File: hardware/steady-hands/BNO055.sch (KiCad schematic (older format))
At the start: 8 parts

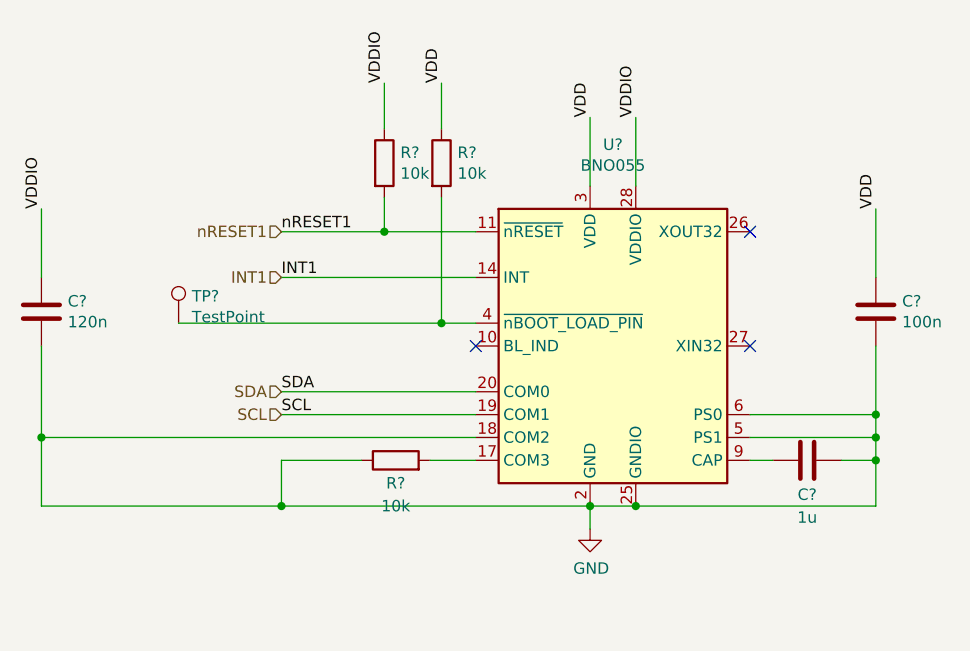
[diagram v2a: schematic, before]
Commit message: Completes schematic connections
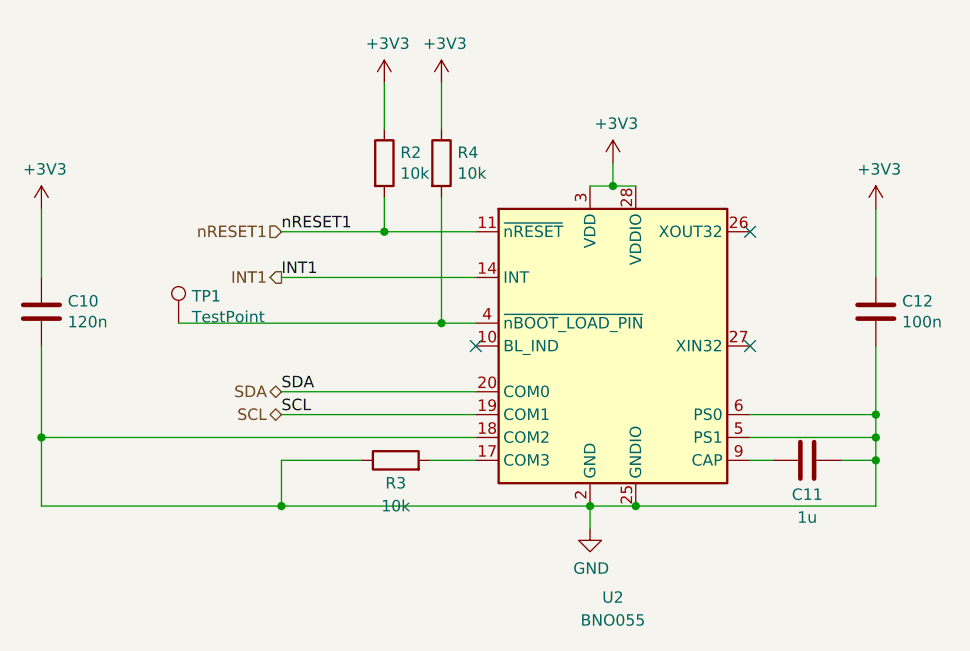
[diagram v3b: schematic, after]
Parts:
- gave numbers to parts that had none: 8
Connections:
- net VDDIO is gone; now on net +3V3: C10.1, R2.1, U2.28 (VDDIO)
- net VDD renamed +3V3
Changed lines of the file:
@@
 $Descr A4 11693 8268
 encoding utf-8
-Sheet 2 7
+Sheet 5 7
 Title ""
 Date ""
@@
 P 6300 3800
 AR Path="/5EF56CFF" Ref="U?"  Part="1"
-AR Path="/5EF43BAC/5EF56CFF" Ref="U?"  Part="1"
-F 0 "U?" H 6300 4681 50  0000 C CNN
-F 1 "BNO055" H 6300 4590 50  0000 C CNN
+AR Path="/5EF43BAC/5EF56CFF" Ref="U2"  Part="1"
+F 0 "U2" H 6300 2700 50  0000 C CNN
+F 1 "BNO055" H 6300 2600 50  0000 C CNN
 F 2 "Package_LGA:LGA-28_5.2x3.8mm_P0.5mm" H 6550 3150 50  0001 L CNN
 F 3 "https://ae-bst.resource.bosch.com/media/_tech/media/datasheets/BST_BNO055_DS000_14.pdf" H 6300 4000 50  0001 C CNN
@@
 $EndComp
 $Comp
-L power:GND #PWR?
+L power:GND #PWR0119
 U 1 1 5EF56D05
 P 6200 4600
-F 0 "#PWR?" H 6200 4350 50  0001 C CNN
+F 0 "#PWR0119" H 6200 4350 50  0001 C CNN
 F 1 "GND" H 6205 4427 50  0000 C CNN
 F 2 "" H 6200 4600 50  0001 C CNN
@@
 Connection ~ 6200 4500
 $Comp
-L Device:C C?
+L Device:C C11
 U 1 1 5EF56D0E
 P 7150 4300
-F 0 "C?" V 7300 4300 50  0000 C CNN
+F 0 "C11" V 7300 4300 50  0000 C CNN
 F 1 "1u" V 7400 4300 50  0000 C CNN
 F 2 "" H 7188 4150 50  0001 C CNN
@@
 Connection ~ 7450 4200
 $Comp
-L Device:R R?
+L Device:R R2
 U 1 1 5EF56D1E
 P 5300 3000
-F 0 "R?" H 5370 3046 50  0000 L CNN
+F 0 "R2" H 5370 3046 50  0000 L CNN
 F 1 "10k" H 5370 2955 50  0000 L CNN
 F 2 "" V 5230 3000 50  0001 C CNN
@@
 $EndComp
 $Comp
-L Device:C C?
+L Device:C C10
 U 1 1 5EF56D2A
 P 3800 3650
-F 0 "C?" H 3915 3696 50  0000 L CNN
+F 0 "C10" H 3915 3696 50  0000 L CNN
 F 1 "120n" H 3915 3605 50  0000 L CNN
 F 2 "" H 3838 3500 50  0001 C CNN
@@
 $EndComp
 $Comp
-L Device:C C?
+L Device:C C12
 U 1 1 5EF56D56
 P 7450 3650
-F 0 "C?" H 7565 3696 50  0000 L CNN
+F 0 "C12" H 7565 3696 50  0000 L CNN
 F 1 "100n" H 7565 3605 50  0000 L CNN
 F 2 "" H 7488 3500 50  0001 C CNN
@@
 	7450 4100 7450 4200
 $Comp
-L Device:R R?
+L Device:R R4
 U 1 1 5EF56D5F
 P 5550 3000
-F 0 "R?" H 5620 3046 50  0000 L CNN
+F 0 "R4" H 5620 3046 50  0000 L CNN
 F 1 "10k" H 5620 2955 50  0000 L CNN
 F 2 "" V 5480 3000 50  0001 C CNN
@@
 Wire Wire Line
 	4850 3500 5700 3500
-Text Label 6400 2800 1    50   ~ 0
-VDDIO
-Text Label 6200 2800 1    50   ~ 0
-VDD
 Text Label 4850 3500 0    50   ~ 0
 INT1
 Text Label 4850 3300 0    50   ~ 0
 nRESET1
-Text Label 5550 2650 1    50   ~ 0
-VDD
-Text Label 7450 3200 1    50   ~ 0
-VDD
-Text Label 3800 3200 1    50   ~ 0
-VDDIO
-Wire Wire Line
-	6400 3100 6400 2800
-Wire Wire Line
-	6200 3100 6200 2800
 Text Label 4850 4100 0    50   ~ 0
 SCL
 Text Label 4850 4000 0    50   ~ 0
 SDA
-Text HLabel 4850 4000 0    50   Input ~ 0
+Text HLabel 4850 4000 0    50   BiDi ~ 0
 SDA
-Text HLabel 4850 4100 0    50   Input ~ 0
+Text HLabel 4850 4100 0    50   BiDi ~ 0
 SCL
-Text HLabel 4850 3500 0    50   Input ~ 0
+Text HLabel 4850 3500 0    50   Output ~ 0
 INT1
 Wire Wire Line
@@
 Wire Wire Line
 	4850 3300 5300 3300
-Text Label 5300 2650 1    50   ~ 0
-VDDIO
 Wire Wire Line
 	5300 2650 5300 2850
@@
 NoConn ~ 5700 3800
 $Comp
-L Connector:TestPoint TP?
+L Connector:TestPoint TP1
 U 1 1 5EFBEA12
 P 4400 3700
-F 0 "TP?" H 4458 3818 50  0000 L CNN
+F 0 "TP1" H 4458 3818 50  0000 L CNN
 F 1 "TestPoint" H 4458 3727 50  0000 L CNN
 F 2 "" H 4600 3700 50  0001 C CNN
@@
 	4400 3700 5550 3700
 $Comp
-L Device:R R?
+L Device:R R3
 U 1 1 5EFC1422
 P 5350 4300
-F 0 "R?" V 5250 4300 50  0000 C CNN
+F 0 "R3" V 5250 4300 50  0000 C CNN
 F 1 "10k" V 5150 4300 50  0000 C CNN
 F 2 "" V 5280 4300 50  0001 C CNN
@@
 Wire Wire Line
 	4850 4500 6200 4500
+Wire Wire Line
+	6200 3100 6300 3100
+Connection ~ 6300 3100
+Wire Wire Line
+	6300 3100 6400 3100
+Wire Wire Line
+	6300 3000 6300 3100
+$Comp
+L power:+3V3 #PWR0120
+U 1 1 5F16055B
+P 6300 3000
+F 0 "#PWR0120" H 6300 2850 50  0001 C CNN
+F 1 "+3V3" H 6315 3173 50  0000 C CNN
+F 2 "" H 6300 3000 50  0001 C CNN
+F 3 "" H 6300 3000 50  0001 C CNN
+	1    6300 3000
+	1    0    0    -1
+$EndComp
+$Comp
+L power:+3V3 #PWR0121
+U 1 1 5F1606C7
+P 7450 3200
+F 0 "#PWR0121" H 7450 3050 50  0001 C CNN
+F 1 "+3V3" H 7465 3373 50  0000 C CNN
+F 2 "" H 7450 3200 50  0001 C CNN
+F 3 "" H 7450 3200 50  0001 C CNN
+	1    7450 3200
+	1    0    0    -1
+$EndComp
+$Comp
+L power:+3V3 #PWR0122
+U 1 1 5F16088A
+P 5550 2650
+F 0 "#PWR0122" H 5550 2500 50  0001 C CNN
+F 1 "+3V3" H 5565 2823 50  0000 C CNN
+F 2 "" H 5550 2650 50  0001 C CNN
+F 3 "" H 5550 2650 50  0001 C CNN
+	1    5550 2650
+	1    0    0    -1
+$EndComp
+$Comp
+L power:+3V3 #PWR0123
+U 1 1 5F160A1A
+P 5300 2650
+F 0 "#PWR0123" H 5300 2500 50  0001 C CNN
+F 1 "+3V3" H 5315 2823 50  0000 C CNN
+F 2 "" H 5300 2650 50  0001 C CNN
+F 3 "" H 5300 2650 50  0001 C CNN
+	1    5300 2650
+	1    0    0    -1
+$EndComp
+$Comp
+L power:+3V3 #PWR0124
+U 1 1 5F160BBC
+P 3800 3200
+F 0 "#PWR0124" H 3800 3050 50  0001 C CNN
+F 1 "+3V3" H 3815 3373 50  0000 C CNN
+F 2 "" H 3800 3200 50  0001 C CNN
+F 3 "" H 3800 3200 50  0001 C CNN
+	1    3800 3200
+	1    0    0    -1
+$EndComp
 $EndSCHEMATC

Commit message: Edits label names and switch configuration
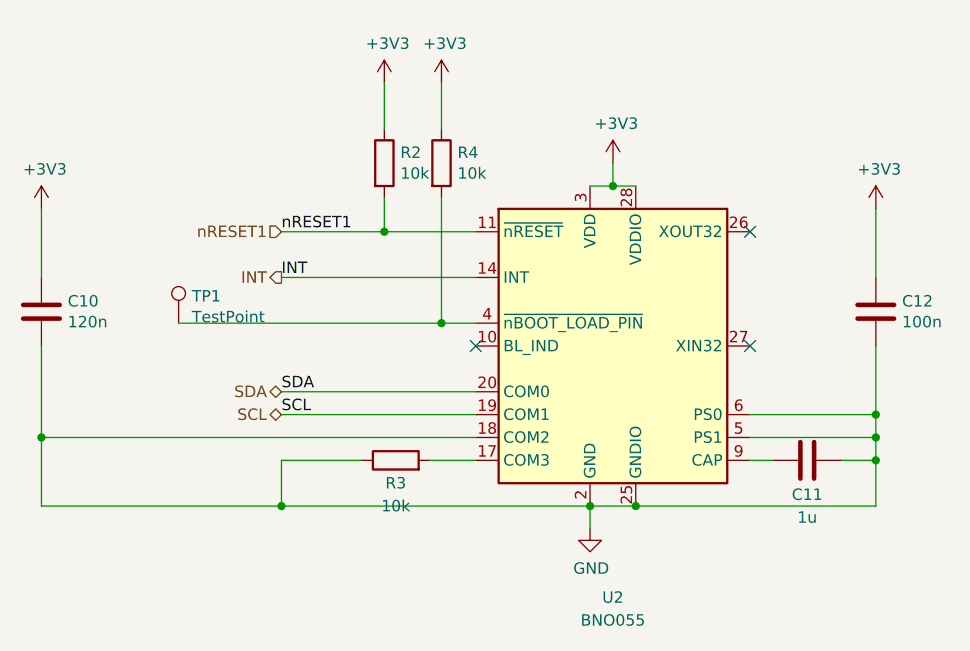
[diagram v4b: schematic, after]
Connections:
- net INT1 renamed INT
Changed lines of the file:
@@
 	4850 3500 5700 3500
 Text Label 4850 3500 0    50   ~ 0
-INT1
+INT
 Text Label 4850 3300 0    50   ~ 0
 nRESET1
@@
 SCL
 Text HLabel 4850 3500 0    50   Output ~ 0
-INT1
+INT
 Wire Wire Line
 	5300 3150 5300 3300

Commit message: Adds footprints
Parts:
- C10, C11, C12: footprint (none) -> Capacitor_SMD:C_0402_1005Metric
- R2, R3, R4: footprint (none) -> Resistor_SMD:R_0402_1005Metric
- TP1: footprint (none) -> TestPoint:TestPoint_Pad_D1.0mm
- U2: symbol Sensor_Motion:BNO055 -> steady-hands-rescue:BNO055-Sensor_Motion
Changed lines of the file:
@@
 $Descr A4 11693 8268
 encoding utf-8
-Sheet 5 7
+Sheet 4 6
 Title ""
 Date ""
@@
 $EndDescr
 $Comp
-L Sensor_Motion:BNO055 U?
+L steady-hands-rescue:BNO055-Sensor_Motion U?
 U 1 1 5EF56CFF
 P 6300 3800
@@
 F 0 "C11" V 7300 4300 50  0000 C CNN
 F 1 "1u" V 7400 4300 50  0000 C CNN
-F 2 "" H 7188 4150 50  0001 C CNN
+F 2 "Capacitor_SMD:C_0402_1005Metric" H 7188 4150 50  0001 C CNN
 F 3 "~" H 7150 4300 50  0001 C CNN
 	1    7150 4300
@@
 F 0 "R2" H 5370 3046 50  0000 L CNN
 F 1 "10k" H 5370 2955 50  0000 L CNN
-F 2 "" V 5230 3000 50  0001 C CNN
+F 2 "Resistor_SMD:R_0402_1005Metric" V 5230 3000 50  0001 C CNN
 F 3 "~" H 5300 3000 50  0001 C CNN
 	1    5300 3000
@@
 F 0 "C10" H 3915 3696 50  0000 L CNN
 F 1 "120n" H 3915 3605 50  0000 L CNN
-F 2 "" H 3838 3500 50  0001 C CNN
+F 2 "Capacitor_SMD:C_0402_1005Metric" H 3838 3500 50  0001 C CNN
 F 3 "~" H 3800 3650 50  0001 C CNN
 	1    3800 3650
@@
 F 0 "C12" H 7565 3696 50  0000 L CNN
 F 1 "100n" H 7565 3605 50  0000 L CNN
-F 2 "" H 7488 3500 50  0001 C CNN
+F 2 "Capacitor_SMD:C_0402_1005Metric" H 7488 3500 50  0001 C CNN
 F 3 "~" H 7450 3650 50  0001 C CNN
 	1    7450 3650
@@
 F 0 "R4" H 5620 3046 50  0000 L CNN
 F 1 "10k" H 5620 2955 50  0000 L CNN
-F 2 "" V 5480 3000 50  0001 C CNN
+F 2 "Resistor_SMD:R_0402_1005Metric" V 5480 3000 50  0001 C CNN
 F 3 "~" H 5550 3000 50  0001 C CNN
 	1    5550 3000
@@
 F 0 "TP1" H 4458 3818 50  0000 L CNN
 F 1 "TestPoint" H 4458 3727 50  0000 L CNN
-F 2 "" H 4600 3700 50  0001 C CNN
+F 2 "TestPoint:TestPoint_Pad_D1.0mm" H 4600 3700 50  0001 C CNN
 F 3 "~" H 4600 3700 50  0001 C CNN
 	1    4400 3700
@@
 F 0 "R3" V 5250 4300 50  0000 C CNN
 F 1 "10k" V 5150 4300 50  0000 C CNN
-F 2 "" V 5280 4300 50  0001 C CNN
+F 2 "Resistor_SMD:R_0402_1005Metric" V 5280 4300 50  0001 C CNN
 F 3 "~" H 5350 4300 50  0001 C CNN
 	1    5350 4300

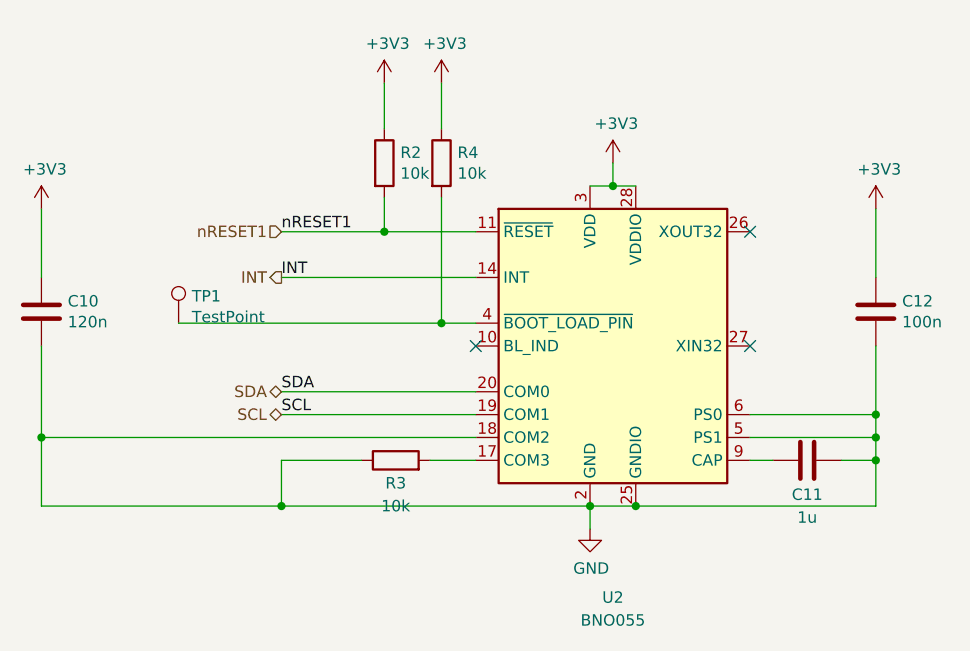
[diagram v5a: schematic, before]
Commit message: Edits PCB layout
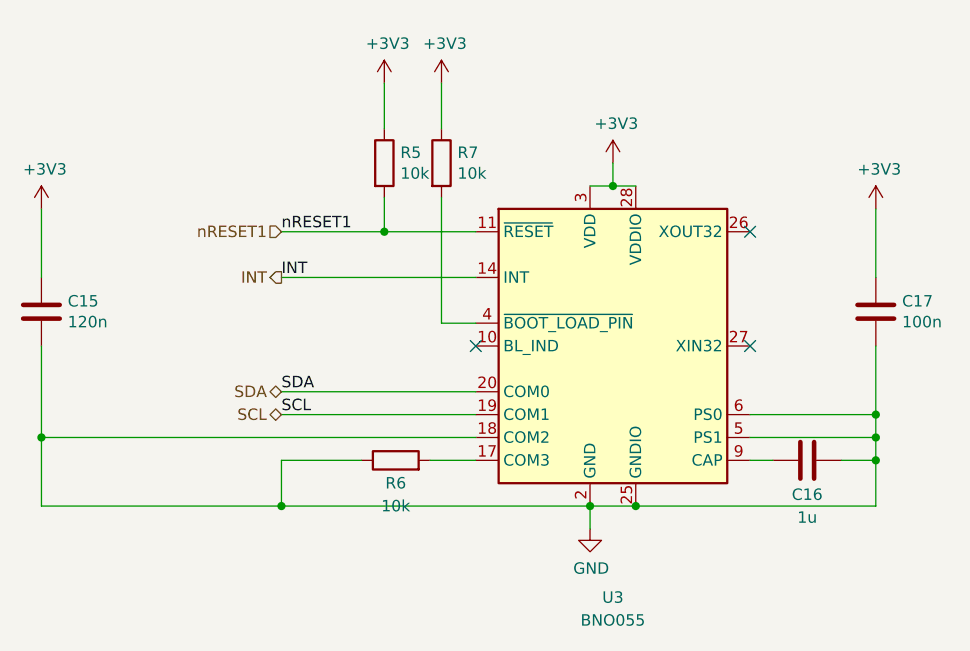
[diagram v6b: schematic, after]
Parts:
- removed TP1: TestPoint, TestPoint:TestPoint_Pad_D1.0mm, symbol Connector:TestPoint
- renumbered C10 to C15, C11 to C16, C12 to C17, R2 to R5, R3 to R6, R4 to R7, U2 to U3
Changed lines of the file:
@@
 P 6300 3800
 AR Path="/5EF56CFF" Ref="U?"  Part="1"
-AR Path="/5EF43BAC/5EF56CFF" Ref="U2"  Part="1"
-F 0 "U2" H 6300 2700 50  0000 C CNN
+AR Path="/5EF43BAC/5EF56CFF" Ref="U3"  Part="1"
+F 0 "U3" H 6300 2700 50  0000 C CNN
 F 1 "BNO055" H 6300 2600 50  0000 C CNN
 F 2 "Package_LGA:LGA-28_5.2x3.8mm_P0.5mm" H 6550 3150 50  0001 L CNN
@@
 $EndComp
 $Comp
-L power:GND #PWR0119
+L power:GND #PWR033
 U 1 1 5EF56D05
 P 6200 4600
-F 0 "#PWR0119" H 6200 4350 50  0001 C CNN
+F 0 "#PWR033" H 6200 4350 50  0001 C CNN
 F 1 "GND" H 6205 4427 50  0000 C CNN
 F 2 "" H 6200 4600 50  0001 C CNN
@@
 Connection ~ 6200 4500
 $Comp
-L Device:C C11
+L Device:C C16
 U 1 1 5EF56D0E
 P 7150 4300
-F 0 "C11" V 7300 4300 50  0000 C CNN
+F 0 "C16" V 7300 4300 50  0000 C CNN
 F 1 "1u" V 7400 4300 50  0000 C CNN
 F 2 "Capacitor_SMD:C_0402_1005Metric" H 7188 4150 50  0001 C CNN
@@
 Connection ~ 7450 4200
 $Comp
-L Device:R R2
+L Device:R R5
 U 1 1 5EF56D1E
 P 5300 3000
-F 0 "R2" H 5370 3046 50  0000 L CNN
+F 0 "R5" H 5370 3046 50  0000 L CNN
 F 1 "10k" H 5370 2955 50  0000 L CNN
 F 2 "Resistor_SMD:R_0402_1005Metric" V 5230 3000 50  0001 C CNN
@@
 $EndComp
 $Comp
-L Device:C C10
+L Device:C C15
 U 1 1 5EF56D2A
 P 3800 3650
-F 0 "C10" H 3915 3696 50  0000 L CNN
+F 0 "C15" H 3915 3696 50  0000 L CNN
 F 1 "120n" H 3915 3605 50  0000 L CNN
 F 2 "Capacitor_SMD:C_0402_1005Metric" H 3838 3500 50  0001 C CNN
@@
 $EndComp
 $Comp
-L Device:C C12
+L Device:C C17
 U 1 1 5EF56D56
 P 7450 3650
-F 0 "C12" H 7565 3696 50  0000 L CNN
+F 0 "C17" H 7565 3696 50  0000 L CNN
 F 1 "100n" H 7565 3605 50  0000 L CNN
 F 2 "Capacitor_SMD:C_0402_1005Metric" H 7488 3500 50  0001 C CNN
@@
 	7450 4100 7450 4200
 $Comp
-L Device:R R4
+L Device:R R7
 U 1 1 5EF56D5F
 P 5550 3000
-F 0 "R4" H 5620 3046 50  0000 L CNN
+F 0 "R7" H 5620 3046 50  0000 L CNN
 F 1 "10k" H 5620 2955 50  0000 L CNN
 F 2 "Resistor_SMD:R_0402_1005Metric" V 5480 3000 50  0001 C CNN
@@
 Text HLabel 4850 3300 0    50   Input ~ 0
 nRESET1
-Connection ~ 5550 3700
 Connection ~ 5300 3300
 Wire Wire Line
@@
 NoConn ~ 5700 3800
 $Comp
-L Connector:TestPoint TP1
-U 1 1 5EFBEA12
-P 4400 3700
-F 0 "TP1" H 4458 3818 50  0000 L CNN
-F 1 "TestPoint" H 4458 3727 50  0000 L CNN
-F 2 "TestPoint:TestPoint_Pad_D1.0mm" H 4600 3700 50  0001 C CNN
-F 3 "~" H 4600 3700 50  0001 C CNN
-	1    4400 3700
-	1    0    0    -1
-$EndComp
-Wire Wire Line
-	4400 3700 5550 3700
-$Comp
-L Device:R R3
+L Device:R R6
 U 1 1 5EFC1422
 P 5350 4300
-F 0 "R3" V 5250 4300 50  0000 C CNN
+F 0 "R6" V 5250 4300 50  0000 C CNN
 F 1 "10k" V 5150 4300 50  0000 C CNN
 F 2 "Resistor_SMD:R_0402_1005Metric" V 5280 4300 50  0001 C CNN
@@
 	6300 3000 6300 3100
 $Comp
-L power:+3V3 #PWR0120
+L power:+3V3 #PWR034
 U 1 1 5F16055B
 P 6300 3000
-F 0 "#PWR0120" H 6300 2850 50  0001 C CNN
+F 0 "#PWR034" H 6300 2850 50  0001 C CNN
 F 1 "+3V3" H 6315 3173 50  0000 C CNN
 F 2 "" H 6300 3000 50  0001 C CNN
@@
 $EndComp
 $Comp
-L power:+3V3 #PWR0121
+L power:+3V3 #PWR035
 U 1 1 5F1606C7
 P 7450 3200
-F 0 "#PWR0121" H 7450 3050 50  0001 C CNN
+F 0 "#PWR035" H 7450 3050 50  0001 C CNN
 F 1 "+3V3" H 7465 3373 50  0000 C CNN
 F 2 "" H 7450 3200 50  0001 C CNN
@@
 $EndComp
 $Comp
-L power:+3V3 #PWR0122
+L power:+3V3 #PWR032
 U 1 1 5F16088A
 P 5550 2650
-F 0 "#PWR0122" H 5550 2500 50  0001 C CNN
+F 0 "#PWR032" H 5550 2500 50  0001 C CNN
 F 1 "+3V3" H 5565 2823 50  0000 C CNN
 F 2 "" H 5550 2650 50  0001 C CNN
@@
 $EndComp
 $Comp
-L power:+3V3 #PWR0123
+L power:+3V3 #PWR031
 U 1 1 5F160A1A
 P 5300 2650
-F 0 "#PWR0123" H 5300 2500 50  0001 C CNN
+F 0 "#PWR031" H 5300 2500 50  0001 C CNN
 F 1 "+3V3" H 5315 2823 50  0000 C CNN
 F 2 "" H 5300 2650 50  0001 C CNN
@@
 $EndComp
 $Comp
-L power:+3V3 #PWR0124
+L power:+3V3 #PWR030
 U 1 1 5F160BBC
 P 3800 3200
-F 0 "#PWR0124" H 3800 3050 50  0001 C CNN
+F 0 "#PWR030" H 3800 3050 50  0001 C CNN
 F 1 "+3V3" H 3815 3373 50  0000 C CNN
 F 2 "" H 3800 3200 50  0001 C CNN
